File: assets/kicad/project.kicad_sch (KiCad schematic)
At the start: 15 parts, among them J1 Micro SD, J2 EPD, J3 RTC, J4 Conn_01x02_Pin, J5 VOUT, J6 VIN, J7 GND, U1 Reset

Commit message: kicad
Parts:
- removed J4: Conn_01x02_Pin, Connector_PinSocket_2.54mm:PinSocket_1x02_P2.54mm_Horizontal, symbol Connector:Conn_01x02_Pin
- removed J5: VOUT, Connector_Pin:Pin_D1.3mm_L10.0mm_W3.5mm_Flat, symbol Connector:Conn_01x01_Pin
- removed J6: VIN, Connector_Pin:Pin_D1.3mm_L10.0mm_W3.5mm_Flat, symbol Connector:Conn_01x01_Pin
- removed J7: GND, Connector_Pin:Pin_D1.3mm_L10.0mm_W3.5mm_Flat, symbol Connector:Conn_01x01_Pin
- removed U1: Reset, Button_Switch_THT:SW_PUSH_6mm, symbol Switch:SW_Push
- added S1: FSMRA6JH, Mouser:P&B Tactile Button Right Angle - FSMRA6JH, symbol Mouser Library:FSMRA6JH
- added S2: OS102011MA1QN1, Mouser:Switch Button - OS102011MA1QN1, symbol Mouser Library:OS102011MA1QN1
- added TP1, TP2: GND, TestPoint:TestPoint_Pad_2.5x2.5mm, symbol Connector:TestPoint
- added TP10: B0, TestPoint:TestPoint_Pad_D2.0mm, symbol Connector:TestPoint
- added TP3: A0/D17, TestPoint:TestPoint_Pad_D2.0mm, symbol Connector:TestPoint
- added TP4: D13/SCK, TestPoint:TestPoint_Pad_D2.0mm, symbol Connector:TestPoint
- added TP5: D2, TestPoint:TestPoint_Pad_D2.0mm, symbol Connector:TestPoint
- added TP6: D1/TX, TestPoint:TestPoint_Pad_D2.0mm, symbol Connector:TestPoint
- added TP7: D0/RX, TestPoint:TestPoint_Pad_D2.0mm, symbol Connector:TestPoint
- added TP8: A6/D23, TestPoint:TestPoint_Pad_D2.0mm, symbol Connector:TestPoint
- added TP9: Hard Reset, TestPoint:TestPoint_2Pads_Pitch2.54mm_Drill0.8mm, symbol Connector:TestPoint_2Pole
- A1: value Arduino_Nano_ESP32 -> Arduino Nano ESP32
- BT1: value Battery_Cell -> Battery In; footprint Connector_JST:JST_PH_B2B-PH-K_1x02_P2.00mm_Vertical -> Connector_JST:JST_PH_S2B-PH-K_1x02_P2.00mm_Horizontal
- C1, C2: value 0.1uF -> 0.1uF 50v
- J1: value Micro SD -> Adafruit microSD
- R1, R2: value R (1M) -> 1MΩ
- RV1: value Potentiometer -> 20K; footprint Potentiometer_THT:Potentiometer_Omeg_PC16BU_Vertical -> Potentiometer_THT:Potentiometer_Alps_RK163_Single_Horizontal
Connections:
- net +4V: now also S2.2; no longer BT1.1 (+)
- net GND: now also S1.1 (COM), S2.1, TP1.1, TP2.1, TP9.2
- net at A1.3 (~{RESET}): now also S1.2 (NO)
- net at A1.1 (D1/TX): now also TP6.1
- net at A1.16 (D13/SCK): now also TP4.1
- net at A1.18 (B0): now also TP10.1
- net at A1.19 (A0): now also TP3.1
- net at A1.2 (D0/RX): now also TP7.1
- net at A1.25 (A6): now also TP8.1
- net at A1.28 (B1): now also TP9.1
- net at A1.5 (D2): now also TP5.1
- new net: BT1.1 (+), S2.3
- no-connect marks 0 -> 8
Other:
- company: (none) -> Alessandro Crugnola
- title: (none) -> Photo Frame
- moved on the sheet: C1, C2, R1, R2, RV1

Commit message: added delay
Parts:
- renumbered R2 to R1, R1 to R2
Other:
- moved on the sheet: S1, TP10, TP4, TP5, TP6, TP7
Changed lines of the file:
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@@
 	)
 	(no_connect
-		(at 135.89 68.58)
+		(at 133.35 69.85)
 	)
 	(no_connect
@@
 	)
 	(no_connect
-		(at 135.89 66.04)
+		(at 133.35 67.31)
 	)
 	(wire
@@
 	(wire
 		(pts
-			(xy 120.65 78.74) (xy 85.09 78.74)
+			(xy 97.79 78.74) (xy 85.09 78.74)
 		)
 		(stroke
@@
 	(wire
 		(pts
-			(xy 26.67 66.04) (xy 26.67 71.12)
+			(xy 29.21 62.23) (xy 29.21 71.12)
 		)
 		(stroke
@@
 	(wire
 		(pts
-			(xy 163.83 113.03) (xy 163.83 68.58)
+			(xy 163.83 113.03) (xy 163.83 69.85)
 		)
 		(stroke
@@
 	(wire
 		(pts
-			(xy 24.13 76.2) (xy 49.53 76.2)
+			(xy 21.59 76.2) (xy 49.53 76.2)
 		)
 		(stroke
@@
 	(wire
 		(pts
-			(xy 163.83 68.58) (xy 161.29 68.58)
+			(xy 163.83 69.85) (xy 158.75 69.85)
 		)
 		(stroke
@@
 	(wire
 		(pts
-			(xy 163.83 66.04) (xy 161.29 66.04)
+			(xy 163.83 67.31) (xy 158.75 67.31)
 		)
 		(stroke
@@
 	(wire
 		(pts
-			(xy 26.67 71.12) (xy 49.53 71.12)
+			(xy 29.21 71.12) (xy 49.53 71.12)
 		)
 		(stroke
@@
 	(wire
 		(pts
-			(xy 163.83 58.42) (xy 163.83 66.04)
+			(xy 163.83 67.31) (xy 163.83 58.42)
 		)
 		(stroke
@@
 	(wire
 		(pts
-			(xy 41.91 104.14) (xy 49.53 104.14)
+			(xy 24.13 104.14) (xy 49.53 104.14)
 		)
 		(stroke
@@
 	(wire
 		(pts
-			(xy 24.13 74.93) (xy 24.13 76.2)
+			(xy 21.59 73.66) (xy 21.59 76.2)
 		)
 		(stroke
@@
 	(wire
 		(pts
-			(xy 41.91 102.87) (xy 41.91 104.14)
+			(xy 24.13 102.87) (xy 24.13 104.14)
 		)
 		(stroke
@@
 	(wire
 		(pts
-			(xy 120.65 62.23) (xy 120.65 78.74)
+			(xy 97.79 76.2) (xy 97.79 78.74)
 		)
 		(stroke
@@
 	(wire
 		(pts
-			(xy 25.4 71.12) (xy 25.4 73.66)
+			(xy 25.4 68.58) (xy 25.4 73.66)
 		)
 		(stroke
@@
 		(dnp no)
 		(fields_autoplaced yes)
-		(property "Reference" "R2"
+		(property "Reference" "R1"
 			(at 191.77 35.56 90)
 			(effects
@@
 			(project ""
 				(path "/f8e09e1c-881e-489b-95e9-2234c93d45c2"
-					(reference "R2")
+					(reference "R1")
 					(unit 1)
 				)
@@
 	(symbol
 		(lib_id "Mouser Library:FSMRA6JH")
-		(at 161.29 68.58 180)
+		(at 158.75 69.85 180)
 		(unit 1)
 		(exclude_from_sim no)
@@
 		(fields_autoplaced yes)
 		(property "Reference" "S1"
-			(at 148.59 58.42 0)
+			(at 146.05 59.69 0)
 			(effects
 				(font
@@
 		)
 		(property "Value" "FSMRA6JH"
-			(at 148.59 60.96 0)
+			(at 146.05 62.23 0)
 			(effects
 				(font
@@
 		)
 		(property "Footprint" "Mouser:P&B Tactile Button Right Angle - FSMRA6JH"
-			(at 139.7 -26.34 0)
+			(at 137.16 -25.07 0)
 			(effects
 				(font
@@
 		)
 		(property "Datasheet" "https://www.te.com/commerce/DocumentDelivery/DDEController?Action=srchrtrv&DocNm=1825027&DocType=Customer%20Drawing&DocLang=English&DocFormat=pdf&PartCntxt=1-1825027-7"
-			(at 139.7 -126.34 0)
+			(at 137.16 -125.07 0)
 			(effects
 				(font
@@
 		)
 		(property "Description" "50 mA Tactile Switch, Round Actuator, NO, Copper Alloy, Silver Contact Plating, Low Profile, 24 VDC, Alcoswitch FSM"
-			(at 162.052 62.23 0)
+			(at 159.512 63.5 0)
 			(effects
 				(font
@@
 		)
 		(property "Height" "7.01"
-			(at 139.7 -326.34 0)
+			(at 137.16 -325.07 0)
 			(effects
 				(font
@@
 		)
 		(property "Mouser Part Number" "655-FSMRA6JH"
-			(at 139.7 -426.34 0)
+			(at 137.16 -425.07 0)
 			(effects
 				(font
@@
 		)
 		(property "Mouser Price/Stock" "https://www.mouser.co.uk/ProductDetail/TE-Connectivity-PB/FSMRA6JH?qs=g%252BEszo6zu8NkDuHQpVqSQA%3D%3D"
-			(at 139.7 -526.34 0)
+			(at 137.16 -525.07 0)
 			(effects
 				(font
@@
 		)
 		(property "Manufacturer_Name" "TE Connectivity"
-			(at 139.7 -626.34 0)
+			(at 137.16 -625.07 0)
 			(effects
 				(font
@@
 		)
 		(property "Manufacturer_Part_Number" "FSMRA6JH"
-			(at 139.7 -726.34 0)
+			(at 137.16 -725.07 0)
 			(effects
 				(font
@@
 	(symbol
 		(lib_id "Connector:TestPoint")
-		(at 25.4 71.12 0)
+		(at 25.4 68.58 0)
 		(unit 1)
 		(exclude_from_sim no)
@@
 		(dnp no)
 		(property "Reference" "TP6"
-			(at 16.002 66.802 0)
+			(at 16.002 64.262 0)
 			(effects
 				(font
@@
 		)
 		(property "Value" "D1/TX"
-			(at 16.002 69.342 0)
+			(at 16.002 66.802 0)
 			(effects
 				(font
@@
 		)
 		(property "Footprint" "TestPoint:TestPoint_Pad_D2.0mm"
-			(at 30.48 71.12 0)
+			(at 30.48 68.58 0)
 			(effects
 				(font
@@
 		)
 		(property "Datasheet" "~"
-			(at 30.48 71.12 0)
+			(at 30.48 68.58 0)
 			(effects
 				(font
@@
 		)
 		(property "Description" "test point"
-			(at 25.4 71.12 0)
+			(at 25.4 68.58 0)
 			(effects
 				(font
@@
 	(symbol
 		(lib_id "Connector:TestPoint")
-		(at 41.91 102.87 0)
+		(at 24.13 102.87 0)
 		(unit 1)
 		(exclude_from_sim no)
@@
 		(dnp no)
 		(property "Reference" "TP4"
-			(at 37.846 103.124 0)
+			(at 20.066 103.124 0)
 			(effects
 				(font
@@
 		)
 		(property "Value" "D13/SCK"
-			(at 37.846 105.664 0)
+			(at 20.066 105.664 0)
 			(effects
 				(font
@@
 		)
 		(property "Footprint" "TestPoint:TestPoint_Pad_D2.0mm"
-			(at 46.99 102.87 0)
+			(at 29.21 102.87 0)
 			(effects
 				(font
@@
 		)
 		(property "Datasheet" "~"
-			(at 46.99 102.87 0)
+			(at 29.21 102.87 0)
 			(effects
 				(font
@@
 		)
 		(property "Description" "test point"
-			(at 41.91 102.87 0)
+			(at 24.13 102.87 0)
 			(effects
 				(font
@@
 	(symbol
 		(lib_id "Connector:TestPoint")
-		(at 120.65 62.23 0)
+		(at 97.79 76.2 0)
 		(unit 1)
 		(exclude_from_sim no)
@@
 		(fields_autoplaced yes)
 		(property "Reference" "TP10"
-			(at 123.19 57.6579 0)
+			(at 100.33 71.6279 0)
 			(effects
 				(font
@@
 		)
 		(property "Value" "B0"
-			(at 123.19 60.1979 0)
+			(at 100.33 74.1679 0)
 			(effects
 				(font
@@
 		)
 		(property "Footprint" "TestPoint:TestPoint_Pad_D2.0mm"
-			(at 125.73 62.23 0)
+			(at 102.87 76.2 0)
 			(effects
 				(font
@@
 		)
 		(property "Datasheet" "~"
-			(at 125.73 62.23 0)
+			(at 102.87 76.2 0)
 			(effects
 				(font
@@
 		)
 		(property "Description" "test point"
-			(at 120.65 62.23 0)
+			(at 97.79 76.2 0)
 			(effects
 				(font
@@
 		(dnp no)
 		(fields_autoplaced yes)
-		(property "Reference" "R1"
+		(property "Reference" "R2"
 			(at 199.39 49.53 90)
 			(effects
@@
 			(project ""
 				(path "/f8e09e1c-881e-489b-95e9-2234c93d45c2"
-					(reference "R1")
+					(reference "R2")
 					(unit 1)
 				)
@@
 	(symbol
 		(lib_id "Connector:TestPoint")
-		(at 26.67 66.04 0)
+		(at 29.21 62.23 0)
 		(unit 1)
 		(exclude_from_sim no)
@@
 		(dnp no)
 		(property "Reference" "TP7"
-			(at 16.002 61.214 0)
+			(at 18.542 57.404 0)
 			(effects
 				(font
@@
 		)
 		(property "Value" "D0/RX"
-			(at 16.002 63.754 0)
+			(at 18.542 59.944 0)
 			(effects
 				(font
@@
 		)
 		(property "Footprint" "TestPoint:TestPoint_Pad_D2.0mm"
-			(at 31.75 66.04 0)
+			(at 34.29 62.23 0)
 			(effects
 				(font
@@
 		)
 		(property "Datasheet" "~"
-			(at 31.75 66.04 0)
+			(at 34.29 62.23 0)
 			(effects
 				(font
@@
 		)
 		(property "Description" "test point"
-			(at 26.67 66.04 0)
+			(at 29.21 62.23 0)
 			(effects
 				(font
@@
 	(symbol
 		(lib_id "Connector:TestPoint")
-		(at 24.13 74.93 0)
+		(at 21.59 73.66 0)
 		(unit 1)
 		(exclude_from_sim no)
@@
 		(dnp no)
 		(property "Reference" "TP5"
-			(at 23.622 77.724 0)
+			(at 17.78 77.216 0)
 			(effects
 				(font
@@
 		)
 		(property "Value" "D2"
-			(at 23.622 80.264 0)
+			(at 17.526 79.502 0)
 			(effects
 				(font
@@
 		)
 		(property "Footprint" "TestPoint:TestPoint_Pad_D2.0mm"
-			(at 29.21 74.93 0)
+			(at 26.67 73.66 0)
 			(effects
 				(font
@@
 		)
 		(property "Datasheet" "~"
-			(at 29.21 74.93 0)
+			(at 26.67 73.66 0)
 			(effects
 				(font
@@
 		)
 		(property "Description" "test point"
-			(at 24.13 74.93 0)
+			(at 21.59 73.66 0)
 			(effects
 				(font

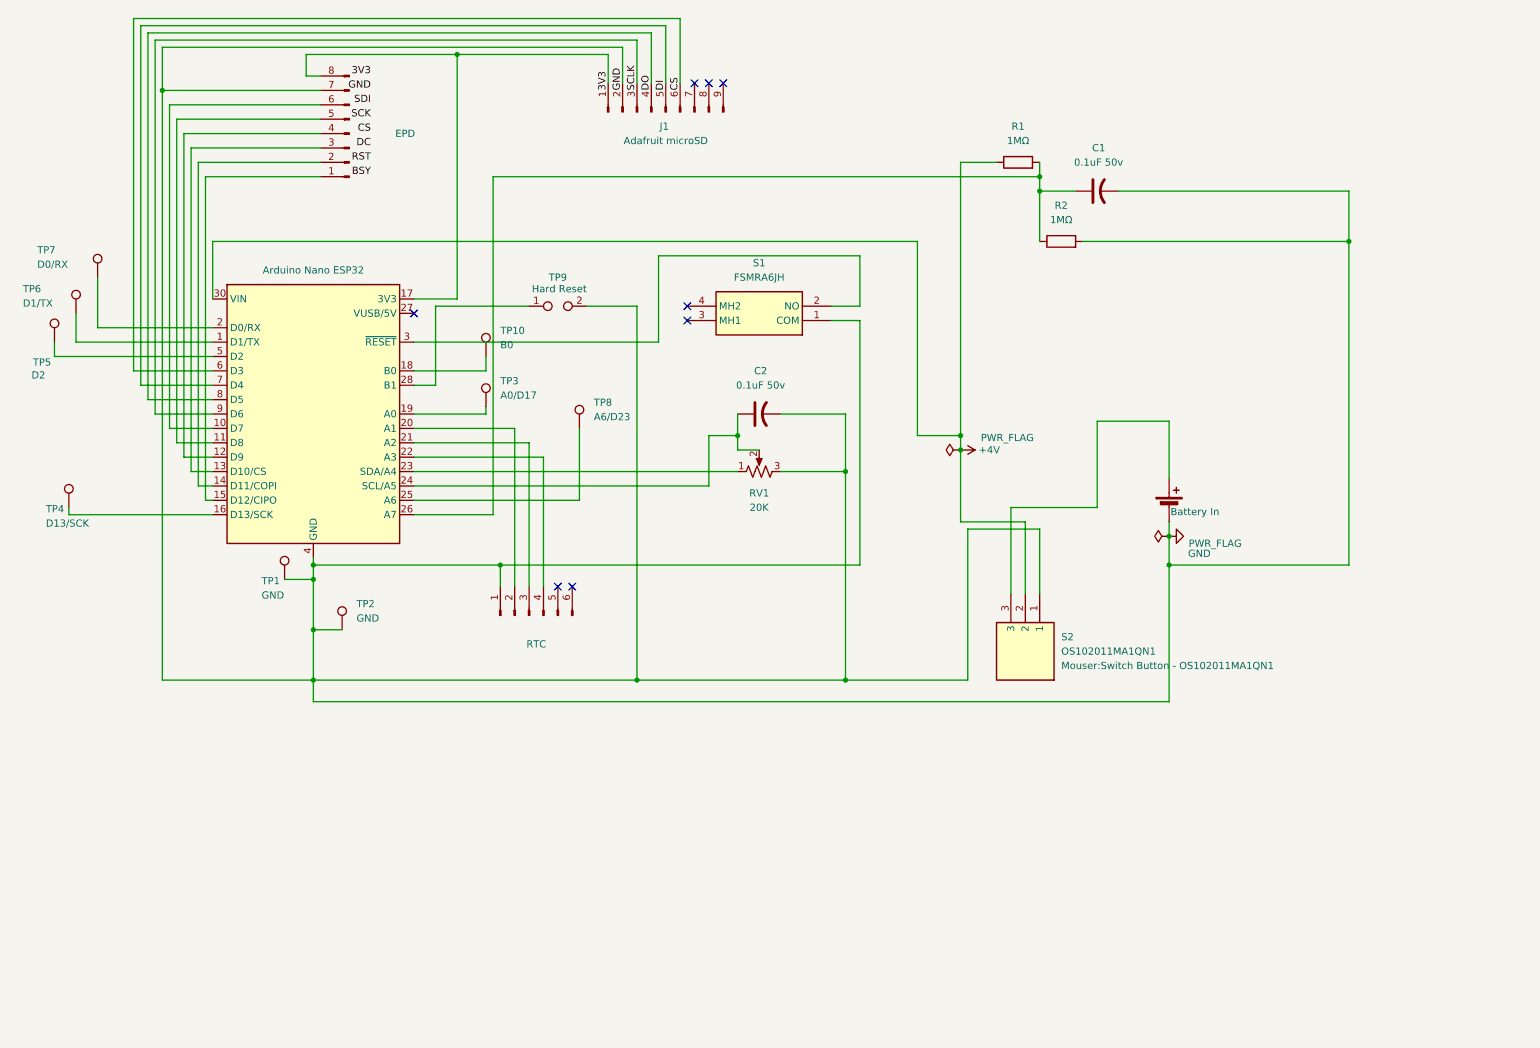
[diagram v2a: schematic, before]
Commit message: updated pins
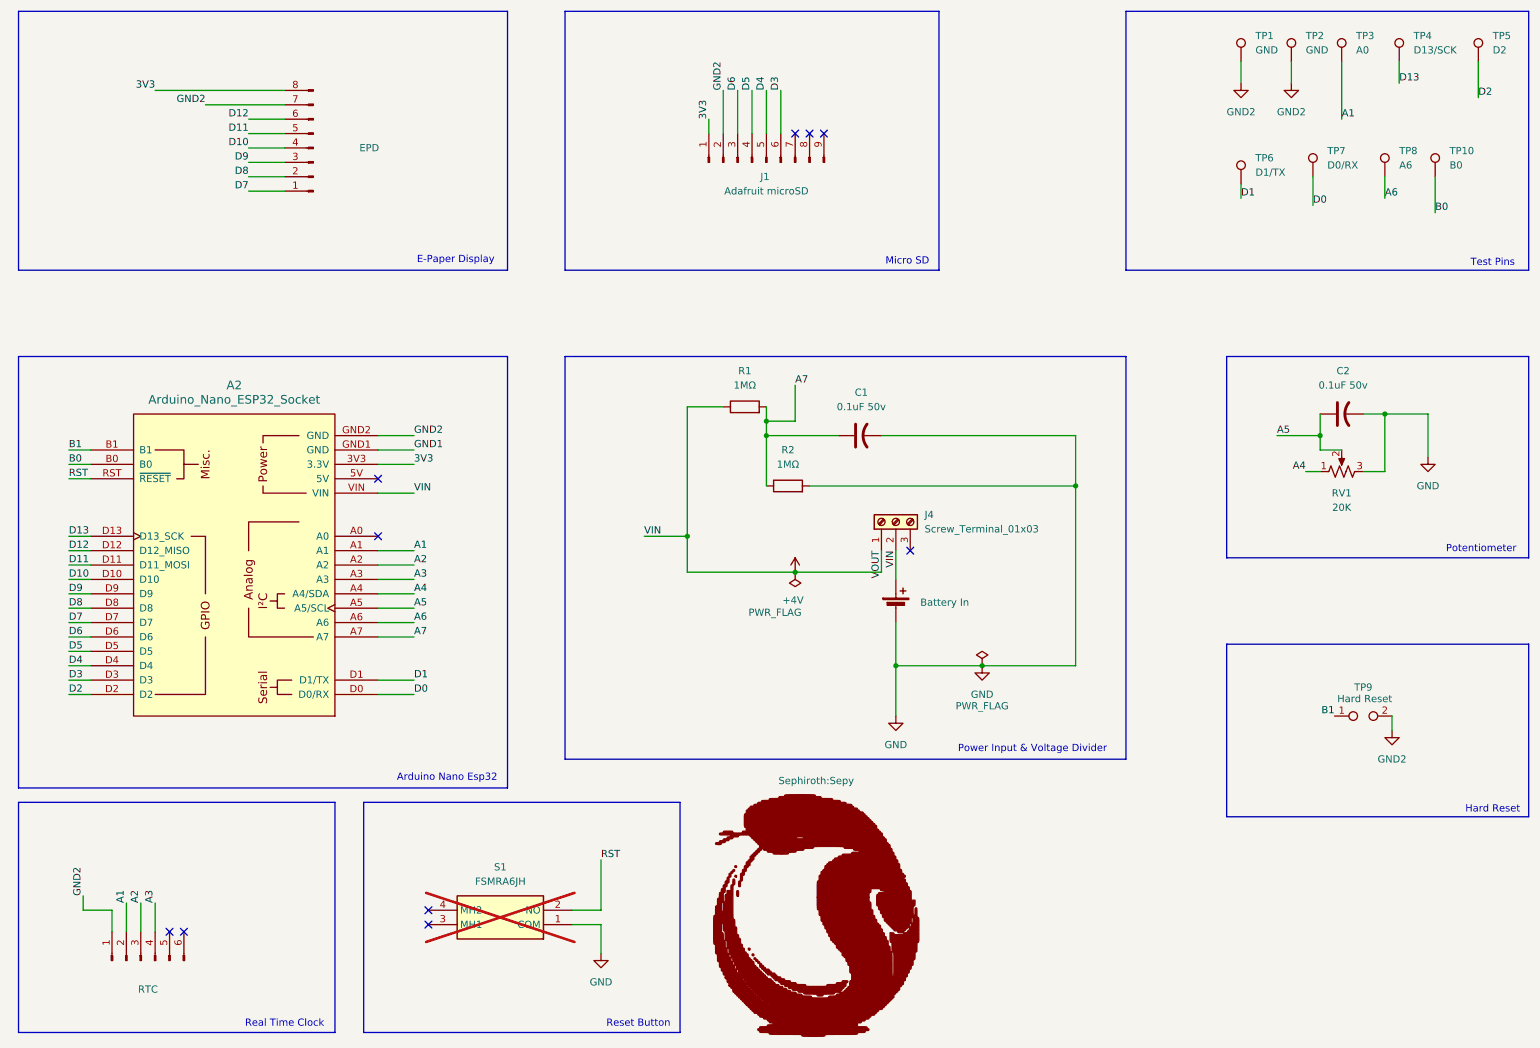
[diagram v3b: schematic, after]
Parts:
- removed A1: Arduino Nano ESP32, Module:Arduino_Nano, symbol MCU_Module:Arduino_Nano_ESP32
- removed S2: OS102011MA1QN1, Mouser:Switch Button - OS102011MA1QN1, symbol Mouser Library:OS102011MA1QN1
- added A2: Arduino_Nano_ESP32_Socket, PCM_arduino-library:Arduino_Nano_ESP32_Socket, symbol Arduino Library:Arduino_Nano_ESP32_Socket
- added J4: Screw_Terminal_01x03, TerminalBlock:TerminalBlock_MaiXu_MX126-5.0-03P_1x03_P5.00mm, symbol Connector:Screw_Terminal_01x03
- S1: now not fitted
- TP1, TP2: footprint TestPoint:TestPoint_Pad_2.5x2.5mm -> Connector_Wire:SolderWire-0.5sqmm_1x01_D0.9mm_OD2.3mm
- TP10, TP4, TP5, TP6, TP7: footprint TestPoint:TestPoint_Pad_D2.0mm -> Connector_Wire:SolderWire-0.5sqmm_1x01_D0.9mm_OD2.3mm
- TP3: value A0/D17 -> A0; footprint TestPoint:TestPoint_Pad_D2.0mm -> Connector_Wire:SolderWire-0.5sqmm_1x01_D0.9mm_OD2.3mm
- TP8: value A6/D23 -> A6; footprint TestPoint:TestPoint_Pad_D2.0mm -> Connector_Wire:SolderWire-0.5sqmm_1x01_D0.9mm_OD2.3mm
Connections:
- net +4V: now also BT1.1 (+), A2.VIN, J4.1 (Pin_1), J4.2 (Pin_2)
- net 3V3: now also J1.1 (Pin_1), J2.8 (Pin_8), A2.3V3 (3.3V)
- net GND: no longer J1.2 (Pin_2), J2.7 (Pin_7), J3.1 (Pin_1), TP1.1, TP2.1, TP9.2
- net RST: now also S1.2 (NO), A2.RST (~{RESET})
- net D6: now reaches J1.3 (Pin_3)
- net D6: now also A2.D6
- net D5: now reaches J1.4 (Pin_4)
- net D5: now also A2.D5
- net D4: now reaches J1.5 (Pin_5)
- net D4: now also A2.D4
- net D3: now reaches J1.6 (Pin_6)
- net D3: now also A2.D3
- net A7: now reaches C1.1, R1.2, R2.1
- net A7: now also A2.A7
- net B1: now reaches TP9.1
- net B1: now also A2.B1
- net A1: now reaches TP3.1
- net A1: now also J3.2 (Pin_2), A2.A1
- net A6: now reaches TP8.1
- net A6: now also A2.A6
- net D1: now reaches TP6.1
- net D1: now also A2.D1 (D1/TX)
- net D13: now reaches TP4.1
- net D13: now also A2.D13 (D13_SCK)
- net B0: now reaches TP10.1
- net B0: now also A2.B0
- net D7: now reaches J2.1 (Pin_1)
- net D7: now also A2.D7
- net D8: now reaches J2.2 (Pin_2)
- net D8: now also A2.D8
- net D9: now reaches J2.3 (Pin_3)
- net D9: now also A2.D9
- net D10: now reaches J2.4 (Pin_4)
- net D10: now also A2.D10
- net D11: now reaches J2.5 (Pin_5)
- net D11: now also A2.D11 (D11_MOSI)
- net D12: now reaches J2.6 (Pin_6)
- net D12: now also A2.D12 (D12_MISO)
- net A5: now reaches C2.1, RV1.2
- net A5: now also A2.A5 (A5/SCL)
- net A4: now reaches RV1.1
- net A4: now also A2.A4 (A4/SDA)
- net D0: now reaches TP7.1
- net D0: now also A2.D0 (D0/RX)
- net A2: now reaches J3.3 (Pin_3)
- net A2: now also A2.A2
- net A3: now reaches J3.4 (Pin_4)
- net A3: now also A2.A3
- net D2: now reaches TP5.1
- net D2: now also A2.D2
- new net GND1: A2.GND1 (GND)
- new net GND2: A2.GND2 (GND), J1.2 (Pin_2), J2.7 (Pin_7), J3.1 (Pin_1), TP1.1, TP2.1, TP9.2
- no-connect marks 8 -> 10
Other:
- note added: "Arduino Nano Esp32"
- note added: "E-Paper Display"
- note added: "Hard Reset"
- note added: "Micro SD"
- note added: "Potentiometer"
- note added: "Power Input & Voltage Divider"
- note added: "Real Time Clock"
- note added: "Reset Button"
- note added: "Test Pins"
- moved on the sheet: C1, C2, J1, R1, R2, RV1, TP1, TP10, TP2, TP3, TP4, TP5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
